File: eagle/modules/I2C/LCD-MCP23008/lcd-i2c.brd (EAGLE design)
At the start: 52.1 x 43.2 mm, 18 parts, among them IC1 MCP2300X/P, J2 RJ12RIGHTANGLE-I2C, J3 RJ12RIGHTANGLE-I2C, Q1 BC349, X2 22-23-2041

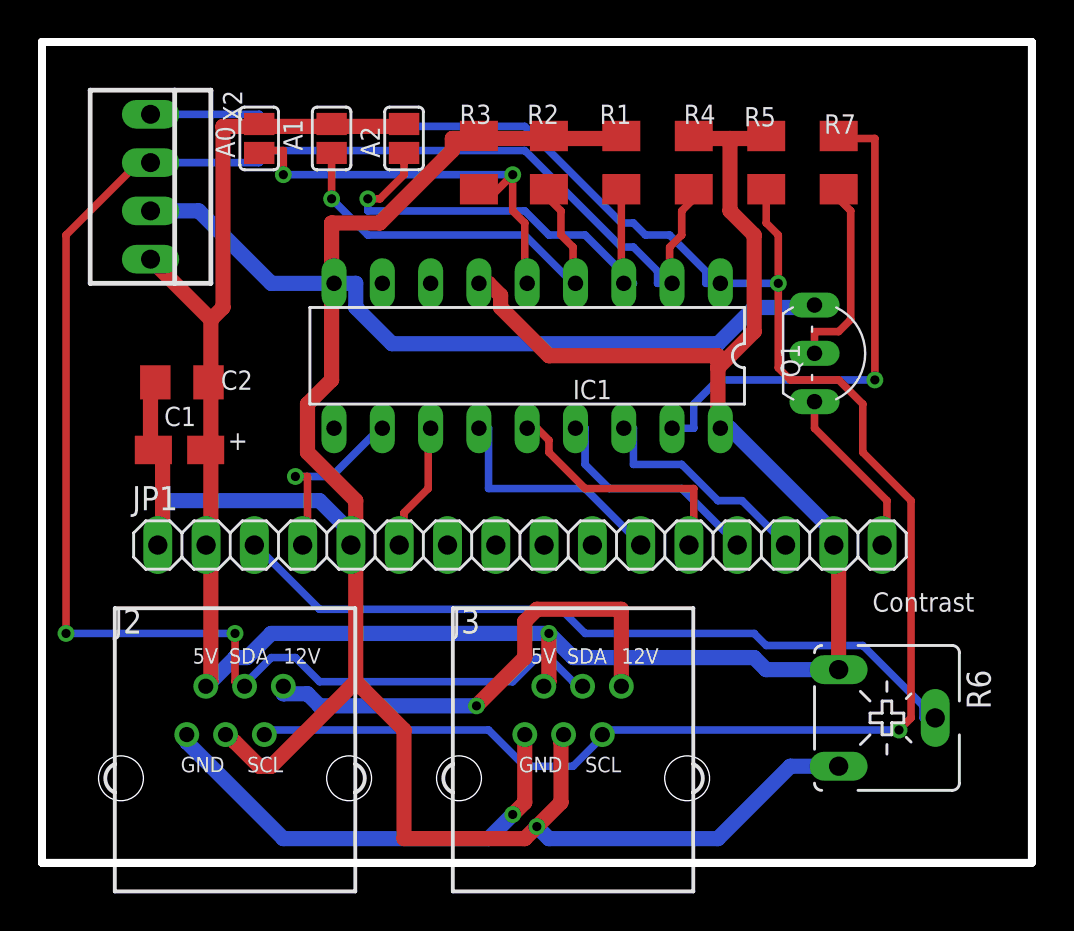
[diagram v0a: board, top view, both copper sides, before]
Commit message: Correct connecter orientation
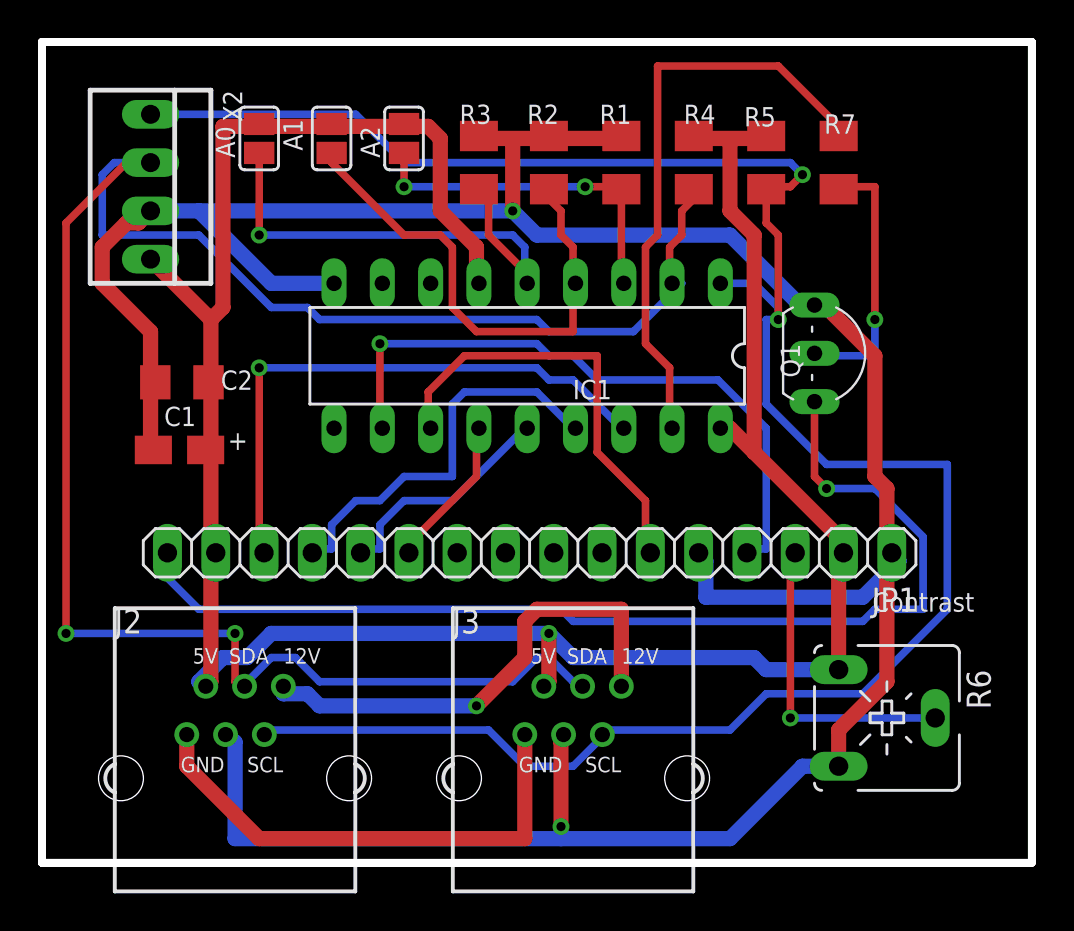
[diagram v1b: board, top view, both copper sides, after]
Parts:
- moved JP1 0.65 mm to (25.7, 16.3), turned to 180 degrees
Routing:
- net N$7: track 9.19 -> 57.2 mm, vias 0 -> 1
- net RS: track 9.94 -> 34.1 mm
- net N$10: track 39.9 -> 16.4 mm, vias 0 -> 1
- net DB7: track 12.2 -> 30.3 mm, vias 0 -> 1
- net E: track 6.87 -> 23.2 mm
- net DATA: track 95.6 -> 105.1 mm
- net DB6: track 12.2 -> 21.1 mm
- net CLOCK: track 105.5 -> 113.0 mm
- net N$3: track 25.3 -> 18.4 mm, vias 1 -> 2
- net DB4: track 12.9 -> 8.22 mm
- net N$2: track 22.7 -> 26.9 mm, vias 1 -> 0
- net LITE: track 27.2 -> 31.3 mm, vias 1 -> 0
- net N$9: track 10.4 -> 14.2 mm, vias 0 -> 1
- net VCC: track 134.8 -> 131.1 mm
- net N$1: track 23.3 -> 26.7 mm, vias 2 -> 1
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
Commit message: update RESET pin to put a resistor of 10k to +5V
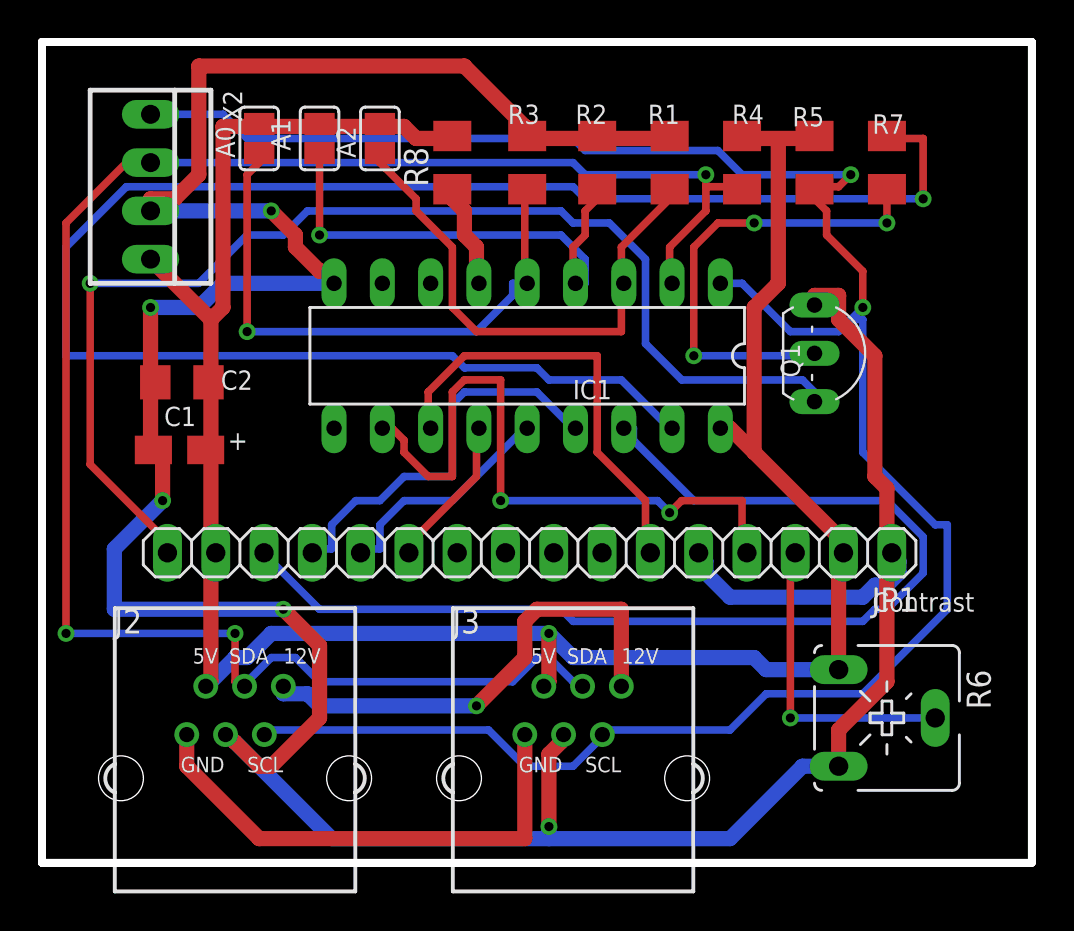
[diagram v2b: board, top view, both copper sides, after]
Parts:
- added R8: 10k, adafruit:M1206
- moved R7 2.54 mm to (44.5, 36.8)
- moved R1 2.54 mm to (33.0, 36.8)
- moved R3 2.54 mm to (25.5, 36.8)
- moved R2 2.54 mm to (29.2, 36.8)
- moved R4 2.54 mm to (36.8, 36.8)
- moved R5 2.54 mm to (40.6, 36.8)
- moved A2 1.27 mm to (17.8, 38.1)
- moved A1 0.63 mm to (14.6, 38.1)
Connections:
- new net N$5: IC1.6, R8.1
- net VCC: now also R8.2; no longer IC1.6
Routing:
- net LITE: track 31.3 -> 91.0 mm, vias 0 -> 1
- net DB7: track 30.3 -> 57.6 mm, vias 1 -> 0
- net GND: track 158.7 -> 182.2 mm, vias 2 -> 5
- net N$9: track 14.2 -> 24.7 mm, vias 1 -> 3
- net N$3: track 18.4 -> 27.8 mm, vias 2 -> 0
- net VCC: track 131.1 -> 122.7 mm
- net DATA: track 105.1 -> 97.6 mm, vias 2 -> 3
- net N$5: track 0.00 -> 5.60 mm
- net N$7: track 57.2 -> 62.6 mm
- net N$1: track 26.7 -> 30.9 mm
- net CLOCK: track 113.0 -> 115.1 mm
- net N$2: track 26.9 -> 26.2 mm, vias 0 -> 1
- net RS: track 34.1 -> 34.8 mm, vias 1 -> 2
